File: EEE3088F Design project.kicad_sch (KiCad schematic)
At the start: 1 part, among them J1 Conn_02x16_Odd_Even

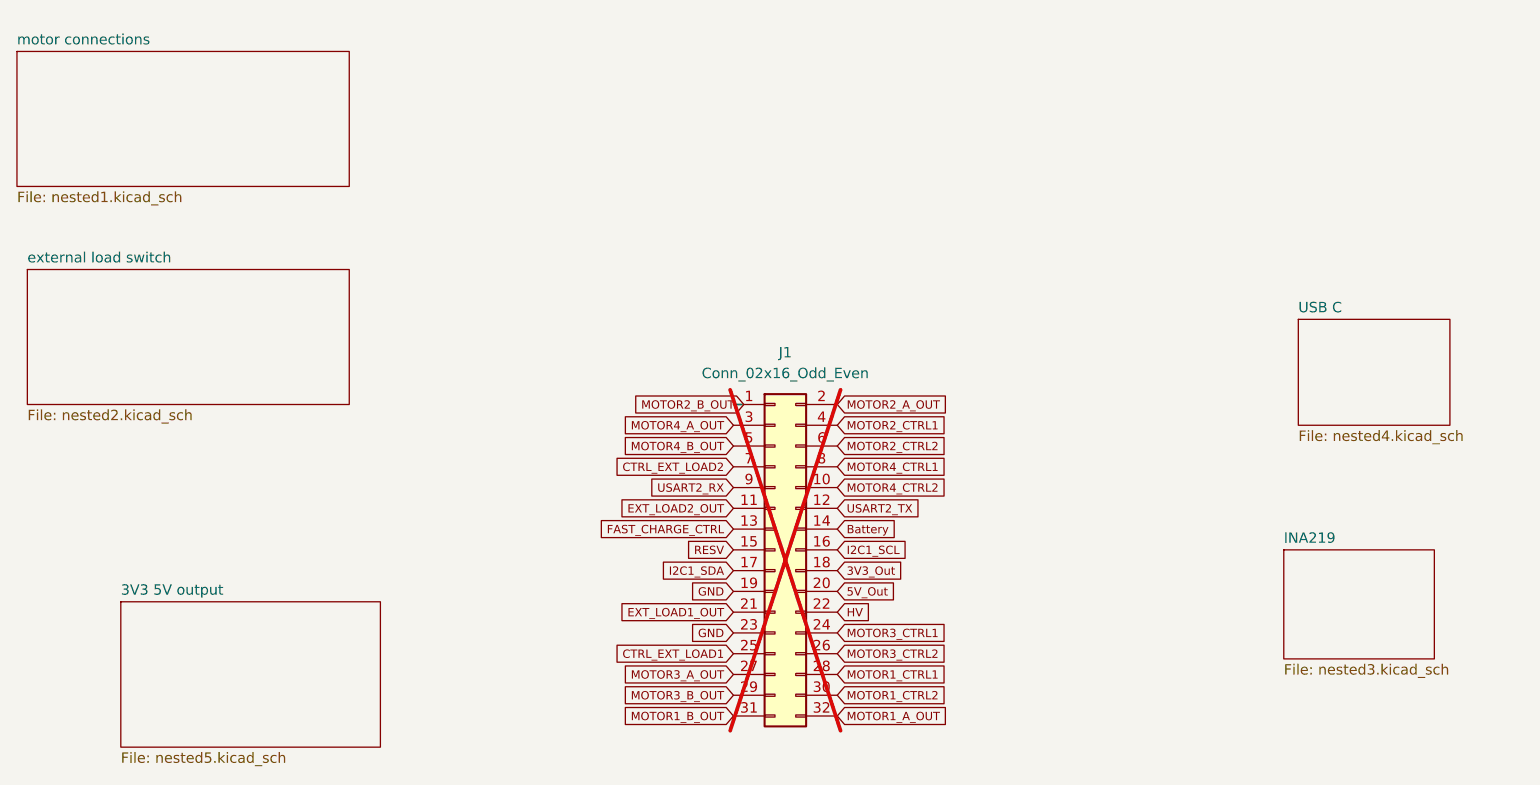
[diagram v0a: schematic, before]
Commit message: Removed old backups and updated KiCad files
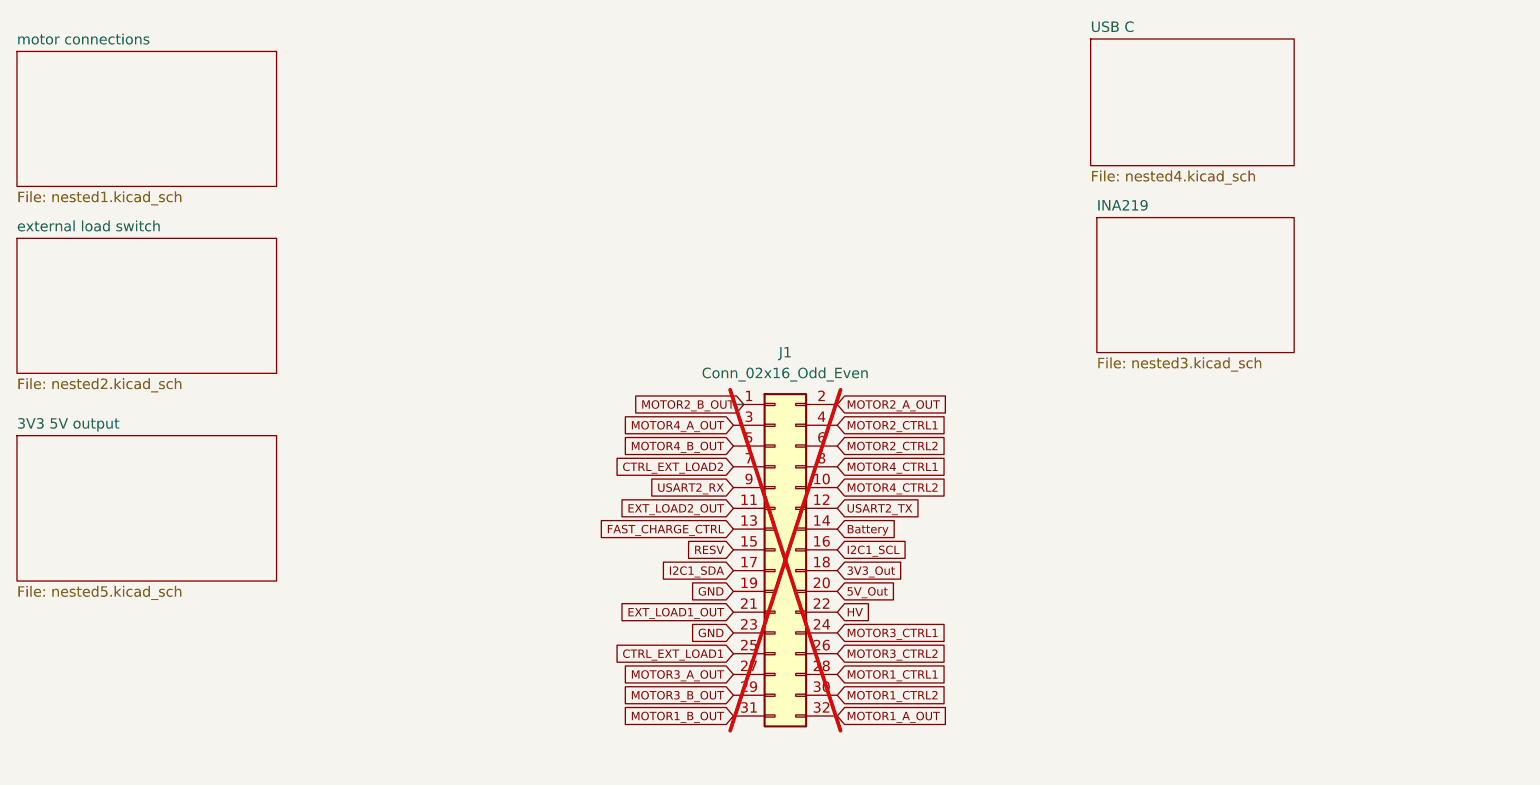
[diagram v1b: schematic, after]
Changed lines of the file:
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@@
 	(sheet
 		(at 53.34 41.91)
-		(size 40.64 16.51)
+		(size 31.75 16.51)
 		(exclude_from_sim no)
 		(in_bom yes)
@@
 	)
 	(sheet
-		(at 54.61 68.58)
-		(size 39.37 16.51)
+		(at 53.34 64.77)
+		(size 31.75 16.51)
 		(exclude_from_sim no)
 		(in_bom yes)
@@
 		)
 		(property "Sheetname" "external load switch"
-			(at 54.61 67.8684 0)
+			(at 53.34 64.0584 0)
 			(show_name yes)
 			(effects
@@
 		)
 		(property "Sheetfile" "nested2.kicad_sch"
-			(at 54.61 85.6746 0)
+			(at 53.34 81.8646 0)
 			(effects
 				(font
@@
 	)
 	(sheet
-		(at 66.04 109.22)
+		(at 53.34 88.9)
 		(size 31.75 17.78)
 		(exclude_from_sim no)
@@
 		)
 		(property "Sheetname" "3V3 5V output"
-			(at 66.04 108.5084 0)
+			(at 53.34 88.1884 0)
 			(effects
 				(font
@@
 		)
 		(property "Sheetfile" "nested5.kicad_sch"
-			(at 66.04 127.5846 0)
+			(at 53.34 107.2646 0)
 			(effects
 				(font
@@
 	)
 	(sheet
-		(at 208.28 102.87)
-		(size 18.415 13.335)
+		(at 185.42 62.23)
+		(size 24.13 16.51)
 		(exclude_from_sim no)
 		(in_bom yes)
@@
 		)
 		(property "Sheetname" "INA219"
-			(at 208.28 102.1584 0)
+			(at 185.42 61.5184 0)
 			(effects
 				(font
@@
 		)
 		(property "Sheetfile" "nested3.kicad_sch"
-			(at 208.28 116.7896 0)
+			(at 185.42 79.3246 0)
 			(effects
 				(font
@@
 			(project "EEE3088F Design project"
 				(path "/d1463c6f-2f5e-4460-8cd2-c7ccf4d8def7"
-					(page "3")
+					(page "4")
 				)
 			)
@@
 	)
 	(sheet
-		(at 210.058 74.676)
-		(size 18.542 12.954)
+		(at 184.658 40.386)
+		(size 24.892 15.494)
 		(exclude_from_sim no)
 		(in_bom yes)
@@
 		)
 		(property "Sheetname" "USB C"
-			(at 210.058 73.9644 0)
+			(at 184.658 39.6744 0)
 			(effects
 				(font
@@
 		)
 		(property "Sheetfile" "nested4.kicad_sch"
-			(at 210.058 88.2146 0)
+			(at 184.658 56.4646 0)
 			(effects
 				(font

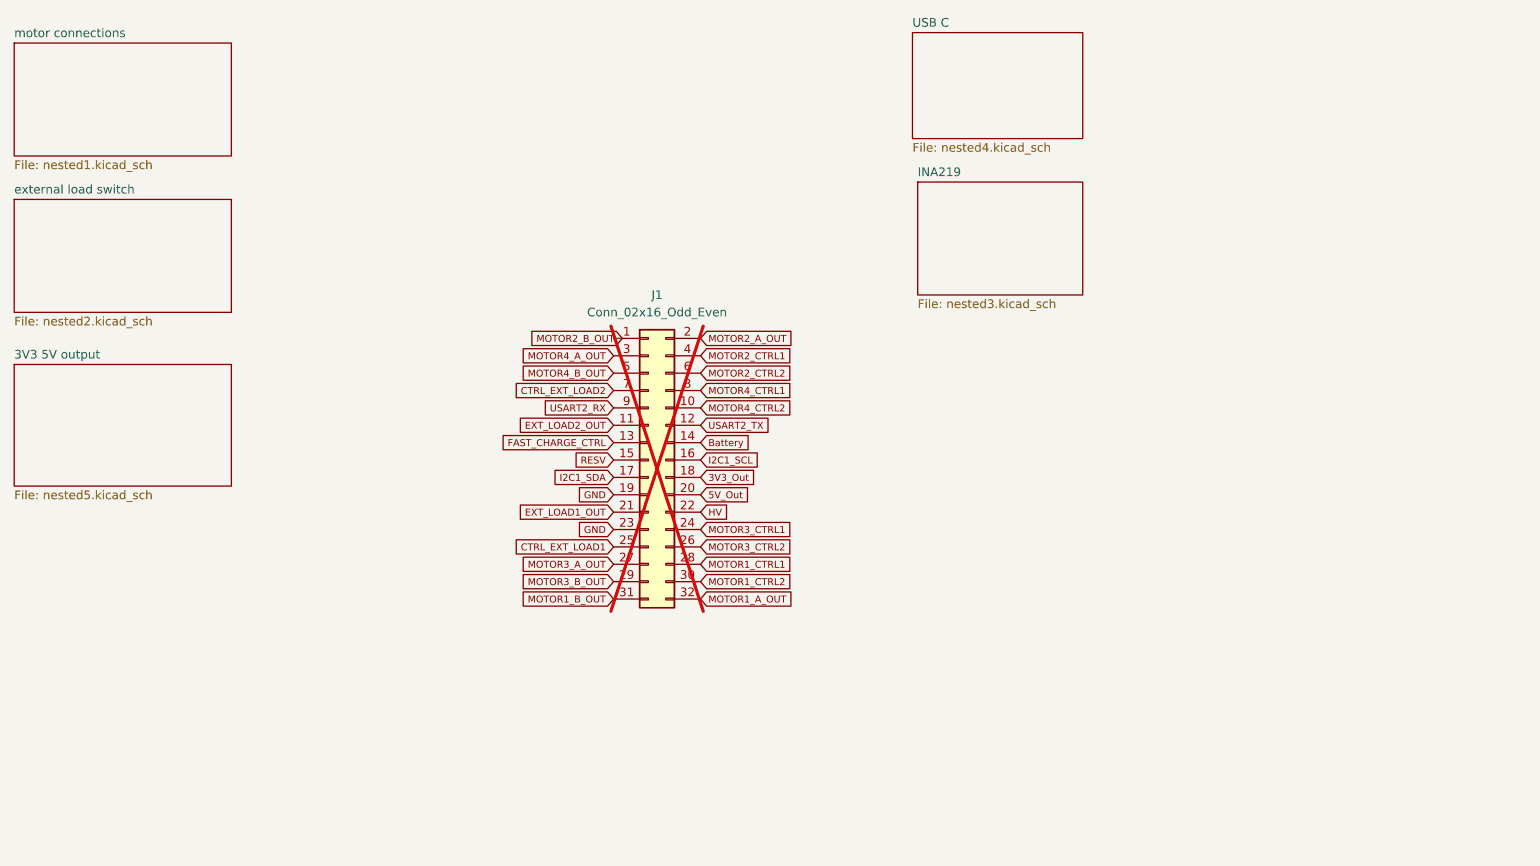
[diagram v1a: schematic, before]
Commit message: Removed old backups and updated KiCad files
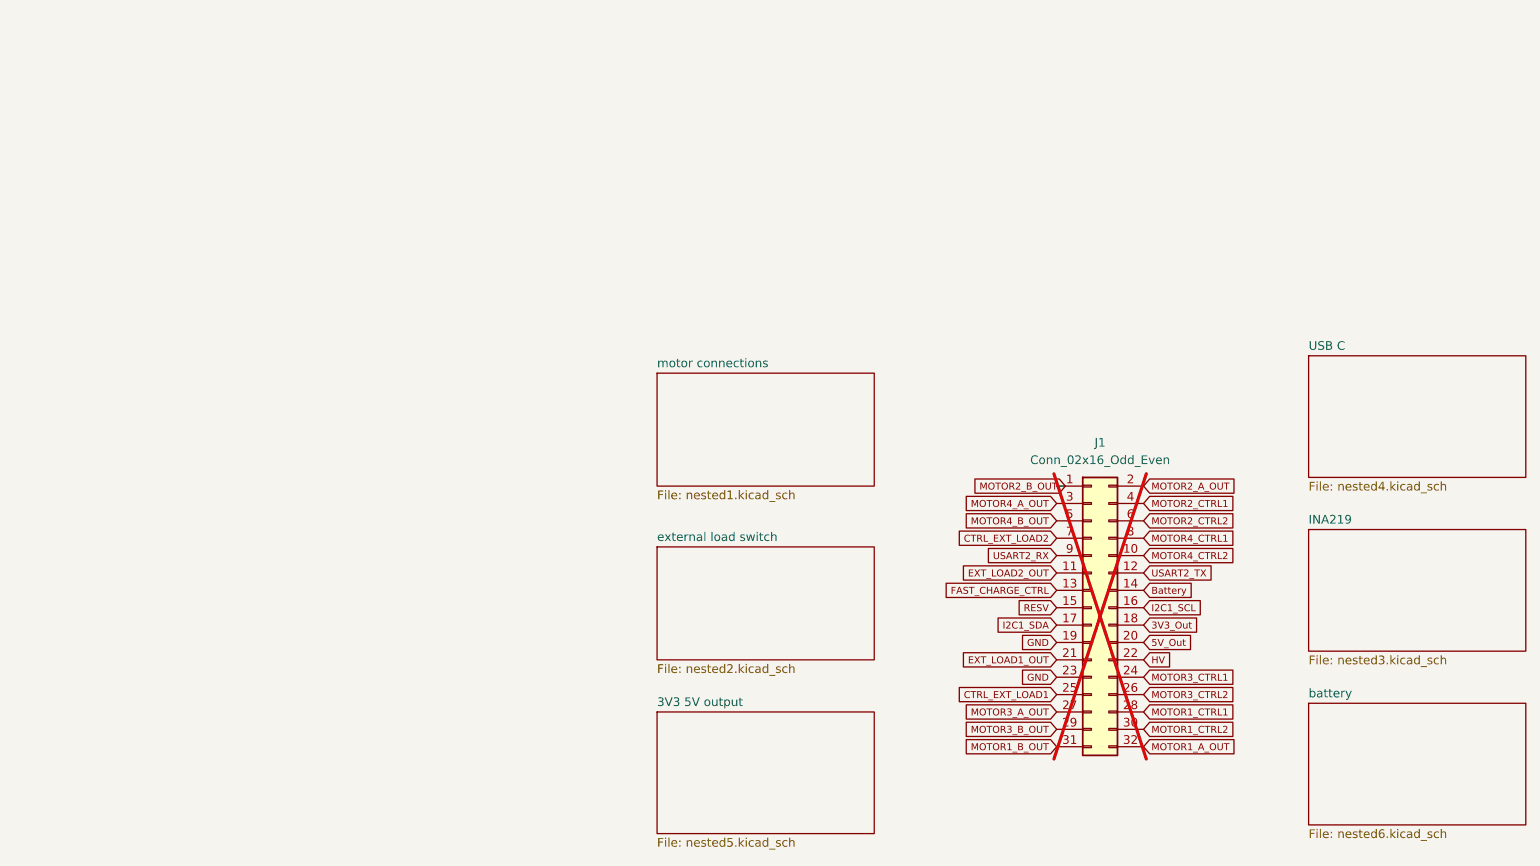
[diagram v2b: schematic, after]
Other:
- added sheet battery (nested6.kicad_sch)
- moved on the sheet: J1

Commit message: footprints added and usb cct finished
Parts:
- J1: footprint (none) -> Connector_PinHeader_2.54mm:PinHeader_2x16_P2.54mm_Vertical
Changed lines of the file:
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@@
 			)
 		)
-		(property "Footprint" ""
+		(property "Footprint" "Connector_PinHeader_2.54mm:PinHeader_2x16_P2.54mm_Vertical"
 			(at 210.82 124.46 0)
 			(effects

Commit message: Removed old backups and update KiCad files
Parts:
- added J4: Conn_01x02, Connector_JST:JST_PH_S2B-PH-K_1x02_P2.00mm_Horizontal, symbol Connector_Generic:Conn_01x02
- J1: now left out of the parts list
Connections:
- net Battery: now also J4.2 (Pin_2)
- net GND: now also J4.1 (Pin_1)
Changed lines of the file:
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@@
+		)
+	)
+	(global_label "GND"
+		(shape input)
+		(at 191.77 90.17 180)
+		(fields_autoplaced yes)
+		(effects
+			(font
+				(size 1.016 1.016)
+			)
+			(justify right)
+		)
+		(property "Intersheetrefs" "${INTERSHEET_REFS}"
+			(at 186.2857 90.17 0)
+			(effects
+				(font
+					(size 1.27 1.27)
+				)
+				(justify right)
+				(hide yes)
+			)
 		)
 	)
@@
 		)
 	)
+	(global_label "Battery"
+		(shape input)
+		(at 191.77 92.71 180)
+		(fields_autoplaced yes)
+		(effects
+			(font
+				(size 1.016 1.016)
+			)
+			(justify right)
+		)
+		(property "Intersheetrefs" "${INTERSHEET_REFS}"
+			(at 184.0117 92.71 0)
+			(effects
+				(font
+					(size 1.27 1.27)
+				)
+				(justify right)
+				(hide yes)
+			)
+		)
+	)
 	(global_label "I2C1_SCL"
 		(shape input)
@@
 				(justify left)
 				(hide yes)
+			)
+		)
+	)
+	(symbol
+		(lib_id "Connector_Generic:Conn_01x02")
+		(at 196.85 90.17 0)
+		(unit 1)
+		(exclude_from_sim no)
+		(in_bom no)
+		(on_board yes)
+		(dnp yes)
+		(fields_autoplaced yes)
+		(property "Reference" "J4"
+			(at 199.39 90.1699 0)
+			(effects
+				(font
+					(size 1.27 1.27)
+				)
+				(justify left)
+			)
+		)
+		(property "Value" "Conn_01x02"
+			(at 199.39 92.7099 0)
+			(effects
+				(font
+					(size 1.27 1.27)
+				)
+				(justify left)
+			)
+		)
+		(property "Footprint" "Connector_JST:JST_PH_S2B-PH-K_1x02_P2.00mm_Horizontal"
+			(at 196.85 90.17 0)
+			(effects
+				(font
+					(size 1.27 1.27)
+				)
+				(hide yes)
+			)
+		)
+		(property "Datasheet" "~"
+			(at 196.85 90.17 0)
+			(effects
+				(font
+					(size 1.27 1.27)
+				)
+				(hide yes)
+			)
+		)
+		(property "Description" "Generic connector, single row, 01x02, script generated (kicad-library-utils/schlib/autogen/connector/)"
+			(at 196.85 90.17 0)
+			(effects
+				(font
+					(size 1.27 1.27)
+				)
+				(hide yes)
+			)
+		)
+		(pin "2"
+		)
+		(pin "1"
+		)
+		(instances
+			(project ""
+				(path "/d1463c6f-2f5e-4460-8cd2-c7ccf4d8def7"
+					(reference "J4")
+					(unit 1)
+				)
 			)
 		)
@@
 		(unit 1)
 		(exclude_from_sim no)
-		(in_bom yes)
+		(in_bom no)
 		(on_board yes)
 		(dnp yes)

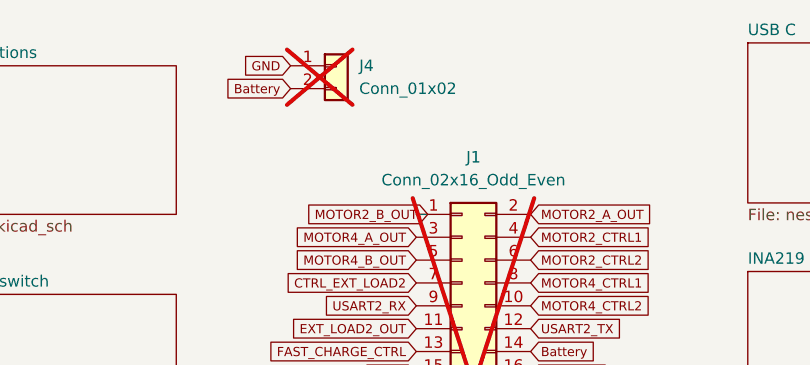
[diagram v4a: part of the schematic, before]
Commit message: Removed old backups and updated KiCad files
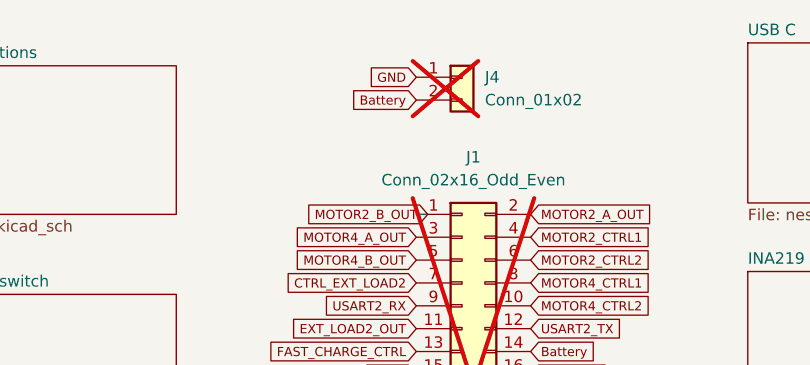
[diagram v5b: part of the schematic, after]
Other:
- moved on the sheet: J4
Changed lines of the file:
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@@
 	(global_label "GND"
 		(shape input)
-		(at 191.77 90.17 180)
-		(fields_autoplaced yes)
-		(effects
-			(font
-				(size 1.016 1.016)
-			)
-			(justify right)
-		)
-		(property "Intersheetrefs" "${INTERSHEET_REFS}"
-			(at 186.2857 90.17 0)
+		(at 205.74 91.44 180)
+		(fields_autoplaced yes)
+		(effects
+			(font
+				(size 1.016 1.016)
+			)
+			(justify right)
+		)
+		(property "Intersheetrefs" "${INTERSHEET_REFS}"
+			(at 200.2557 91.44 0)
 			(effects
 				(font
@@
 	(global_label "Battery"
 		(shape input)
-		(at 191.77 92.71 180)
-		(fields_autoplaced yes)
-		(effects
-			(font
-				(size 1.016 1.016)
-			)
-			(justify right)
-		)
-		(property "Intersheetrefs" "${INTERSHEET_REFS}"
-			(at 184.0117 92.71 0)
+		(at 205.74 93.98 180)
+		(fields_autoplaced yes)
+		(effects
+			(font
+				(size 1.016 1.016)
+			)
+			(justify right)
+		)
+		(property "Intersheetrefs" "${INTERSHEET_REFS}"
+			(at 197.9817 93.98 0)
 			(effects
 				(font
@@
 	(symbol
 		(lib_id "Connector_Generic:Conn_01x02")
-		(at 196.85 90.17 0)
+		(at 210.82 91.44 0)
 		(unit 1)
 		(exclude_from_sim no)
@@
 		(fields_autoplaced yes)
 		(property "Reference" "J4"
-			(at 199.39 90.1699 0)
+			(at 213.36 91.4399 0)
 			(effects
 				(font
@@
 		)
 		(property "Value" "Conn_01x02"
-			(at 199.39 92.7099 0)
+			(at 213.36 93.9799 0)
 			(effects
 				(font
@@
 		)
 		(property "Footprint" "Connector_JST:JST_PH_S2B-PH-K_1x02_P2.00mm_Horizontal"
-			(at 196.85 90.17 0)
+			(at 210.82 91.44 0)
 			(effects
 				(font
@@
 		)
 		(property "Datasheet" "~"
-			(at 196.85 90.17 0)
+			(at 210.82 91.44 0)
 			(effects
 				(font
@@
 		)
 		(property "Description" "Generic connector, single row, 01x02, script generated (kicad-library-utils/schlib/autogen/connector/)"
-			(at 196.85 90.17 0)
-			(effects
-				(font
+			(at 210.82 91.44 0)
+			(effects
+				(font
